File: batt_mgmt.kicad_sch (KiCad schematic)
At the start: 49 parts, among them Q1 DMN2014LHAB-7, Q2 DMP3056L, U1 BQ24074RGT, U2 BQ29728, U3 BQ27427

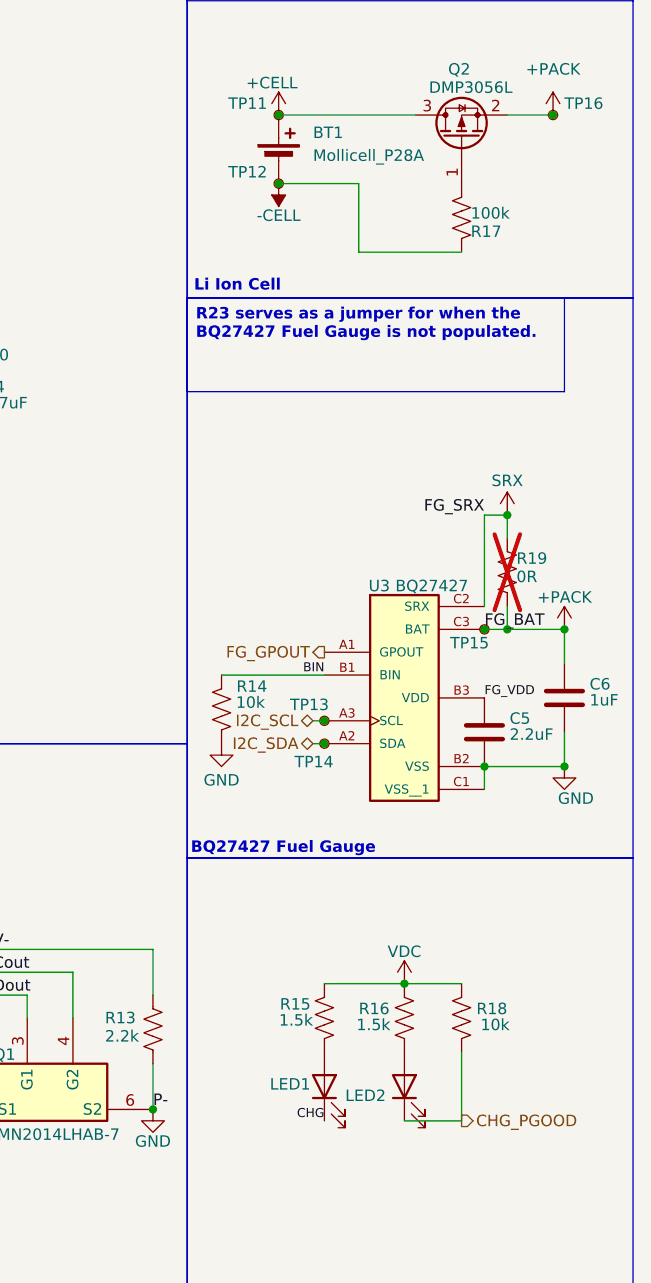
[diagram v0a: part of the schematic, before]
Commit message: Added labels and schematic PDF among other progress
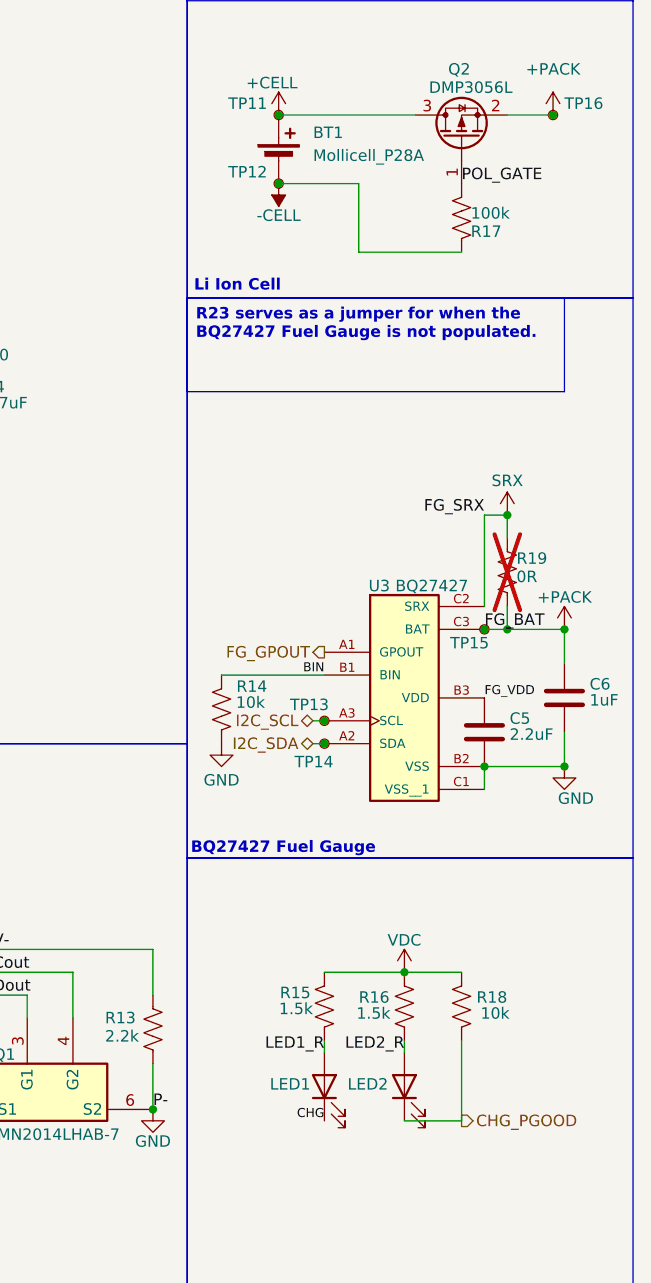
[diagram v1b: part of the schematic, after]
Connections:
- net LED2_R: now reaches LED2.2 (A), R16.1
- net LED1_R: now reaches LED1.2 (A), R15.1
- net POL_GATE: now reaches Q2.1 (G), R17.2
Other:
- moved on the sheet: R15, R16, R18
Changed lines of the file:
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@@
 	)
 	(junction
-		(at 233.68 135.89)
+		(at 233.68 134.62)
 		(diameter 0)
 		(color 0 0 0 0)
@@
 	(wire
 		(pts
-			(xy 233.68 135.89) (xy 240.03 135.89)
+			(xy 233.68 134.62) (xy 240.03 134.62)
 		)
 		(stroke
@@
 	(wire
 		(pts
-			(xy 224.79 135.89) (xy 233.68 135.89)
+			(xy 224.79 134.62) (xy 233.68 134.62)
 		)
 		(stroke
@@
 	(wire
 		(pts
+			(xy 224.79 142.24) (xy 224.79 143.51)
+		)
+		(stroke
+			(width 0)
+			(type default)
+		)
+	)
+	(wire
+		(pts
 			(xy 205.74 144.78) (xy 205.74 149.86)
 		)
@@
 	(wire
 		(pts
-			(xy 240.03 143.51) (xy 240.03 151.13)
+			(xy 240.03 142.24) (xy 240.03 151.13)
 		)
 		(stroke
@@
 	(wire
 		(pts
+			(xy 233.68 142.24) (xy 233.68 143.51)
+		)
+		(stroke
+			(width 0)
+			(type default)
+		)
+	)
+	(wire
+		(pts
 			(xy 242.57 83.82) (xy 245.11 83.82)
 		)
@@
 		)
 	)
+	(label "LED1_R"
+		(at 224.79 143.51 180)
+		(effects
+			(font
+				(size 1.27 1.27)
+			)
+			(justify right bottom)
+		)
+	)
 	(label "P-"
 		(at 205.74 149.86 0)
@@
 		)
 	)
+	(label "LED2_R"
+		(at 233.68 143.51 180)
+		(effects
+			(font
+				(size 1.27 1.27)
+			)
+			(justify right bottom)
+		)
+	)
 	(label "CHG"
 		(at 224.79 151.13 180)
@@
 		)
 	)
+	(label "POL_GATE"
+		(at 240.03 46.99 0)
+		(effects
+			(font
+				(size 1.27 1.27)
+			)
+			(justify left bottom)
+		)
+	)
 	(hierarchical_label "FG_GPOUT"
 		(shape output)
@@
 		(dnp no)
 		(property "Reference" "LED2"
-			(at 229.362 148.336 90)
+			(at 229.616 147.066 90)
 			(show_name no)
 			(do_not_autoplace no)
@@
 	(symbol
 		(lib_id "Device:R_US")
-		(at 240.03 139.7 0)
+		(at 240.03 138.43 0)
 		(mirror x)
 		(unit 1)
@@
 		(dnp no)
 		(property "Reference" "R18"
-			(at 245.11 138.684 0)
+			(at 245.11 137.414 0)
 			(show_name no)
 			(do_not_autoplace no)
@@
 		)
 		(property "Value" "10k"
-			(at 245.364 140.462 0)
+			(at 245.364 139.192 0)
 			(show_name no)
 			(do_not_autoplace no)
@@
 		)
 		(property "Footprint" "Resistor_SMD:R_0603_1608Metric"
-			(at 241.046 139.446 90)
+			(at 241.046 138.176 90)
 			(hide yes)
 			(show_name no)
@@
 		)
 		(property "Datasheet" ""
-			(at 240.03 139.7 0)
+			(at 240.03 138.43 0)
 			(hide yes)
 			(show_name no)
@@
 		)
 		(property "Description" "Resistor, US symbol"
-			(at 240.03 139.7 0)
+			(at 240.03 138.43 0)
 			(hide yes)
 			(show_name no)
@@
 		)
 		(property "MFR#" ""
-			(at 240.03 139.7 0)
+			(at 240.03 138.43 0)
 			(hide yes)
 			(show_name no)
@@
 		)
 		(property "Package" "0603"
-			(at 240.03 139.7 0)
+			(at 240.03 138.43 0)
 			(hide yes)
 			(show_name no)
@@
 		)
 		(property "LCSC#" "C98220"
-			(at 240.03 139.7 0)
+			(at 240.03 138.43 0)
 			(hide yes)
 			(show_name no)
@@
 	(symbol
 		(lib_id "Device:R_US")
-		(at 233.68 139.7 180)
+		(at 233.68 138.43 180)
 		(unit 1)
 		(body_style 1)
@@
 		(dnp no)
 		(property "Reference" "R16"
-			(at 228.6 138.684 0)
+			(at 228.6 137.414 0)
 			(show_name no)
 			(do_not_autoplace no)
@@
 		)
 		(property "Value" "1.5k"
-			(at 228.346 140.462 0)
+			(at 228.346 139.192 0)
 			(show_name no)
 			(do_not_autoplace no)
@@
 		)
 		(property "Footprint" "Resistor_SMD:R_0603_1608Metric"
-			(at 232.664 139.446 90)
+			(at 232.664 138.176 90)
 			(hide yes)
 			(show_name no)
@@
 		)
 		(property "Datasheet" ""
-			(at 233.68 139.7 0)
+			(at 233.68 138.43 0)
 			(hide yes)
 			(show_name no)
@@
 		)
 		(property "Description" "Resistor, US symbol"
-			(at 233.68 139.7 0)
+			(at 233.68 138.43 0)
 			(hide yes)
 			(show_name no)
@@
 		)
 		(property "MFR#" ""
-			(at 233.68 139.7 0)
+			(at 233.68 138.43 0)
 			(hide yes)
 			(show_name no)
@@
 		)
 		(property "Package" "0603"
-			(at 233.68 139.7 0)
+			(at 233.68 138.43 0)
 			(hide yes)
 			(show_name no)
@@
 		)
 		(property "LCSC#" "C114680"
-			(at 233.68 139.7 0)
+			(at 233.68 138.43 0)
 			(hide yes)
 			(show_name no)
@@
 	(symbol
 		(lib_id "power:VDC")
-		(at 233.68 135.89 0)
+		(at 233.68 134.62 0)
 		(unit 1)
 		(body_style 1)
@@
 		(dnp no)
 		(property "Reference" "#PWR018"
-			(at 233.68 139.7 0)
+			(at 233.68 138.43 0)
 			(hide yes)
 			(show_name no)
@@
 		)
 		(property "Value" "VDC"
-			(at 233.68 132.334 0)
+			(at 233.68 131.064 0)
 			(show_name no)
 			(do_not_autoplace no)
@@
 		)
 		(property "Footprint" ""
-			(at 233.68 135.89 0)
+			(at 233.68 134.62 0)
 			(hide yes)
 			(show_name no)
@@
 		)
 		(property "Datasheet" ""
-			(at 233.68 135.89 0)
+			(at 233.68 134.62 0)
 			(hide yes)
 			(show_name no)
@@
 		)
 		(property "Description" "Power symbol creates a global label with name \"VDC\""
-			(at 233.68 135.89 0)
+			(at 233.68 134.62 0)
 			(hide yes)
 			(show_name no)
@@
 	(symbol
 		(lib_id "Device:R_US")
-		(at 224.79 139.7 0)
+		(at 224.79 138.43 0)
 		(mirror x)
 		(unit 1)
@@
 		(dnp no)
 		(property "Reference" "R15"
-			(at 223.266 138.176 0)
+			(at 223.266 136.906 0)
 			(show_name no)
 			(do_not_autoplace no)
@@
 		)
 		(property "Value" "1.5k"
-			(at 223.52 139.954 0)
+			(at 223.52 138.684 0)
 			(show_name no)
 			(do_not_autoplace no)
@@
 		)
 		(property "Footprint" "Resistor_SMD:R_0603_1608Metric"
-			(at 225.806 139.446 90)
+			(at 225.806 138.176 90)
 			(hide yes)
 			(show_name no)
@@
 		)
 		(property "Datasheet" ""
-			(at 224.79 139.7 0)
+			(at 224.79 138.43 0)
 			(hide yes)
 			(show_name no)
@@
 		)
 		(property "Description" "Resistor, US symbol"
-			(at 224.79 139.7 0)
+			(at 224.79 138.43 0)
 			(hide yes)
 			(show_name no)
@@
 		)
 		(property "MFR#" ""
-			(at 224.79 139.7 0)
+			(at 224.79 138.43 0)
 			(hide yes)
 			(show_name no)
@@
 		)
 		(property "Package" "0603"
-			(at 224.79 139.7 0)
+			(at 224.79 138.43 0)
 			(hide yes)
 			(show_name no)
@@
 		)
 		(property "LCSC#" "C114680"
-			(at 224.79 139.7 0)
+			(at 224.79 138.43 0)
 			(hide yes)
 			(show_name no)

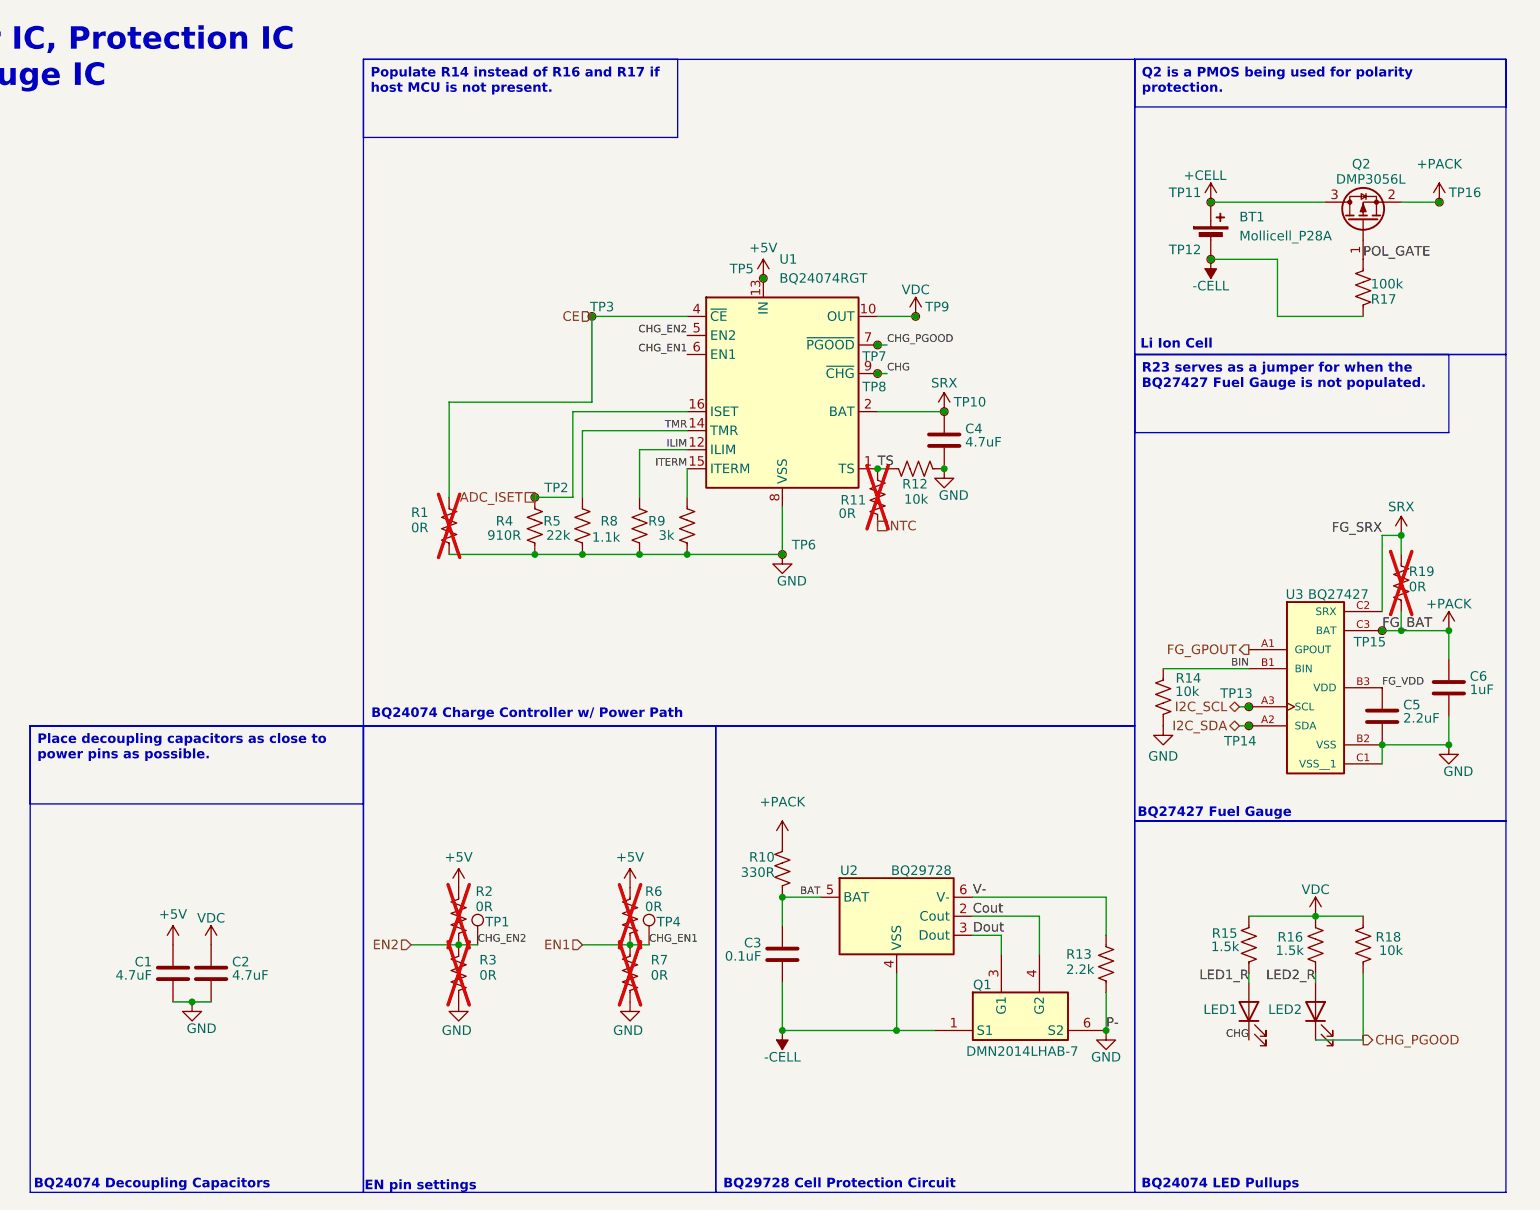
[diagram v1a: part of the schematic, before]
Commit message: Added testpoints
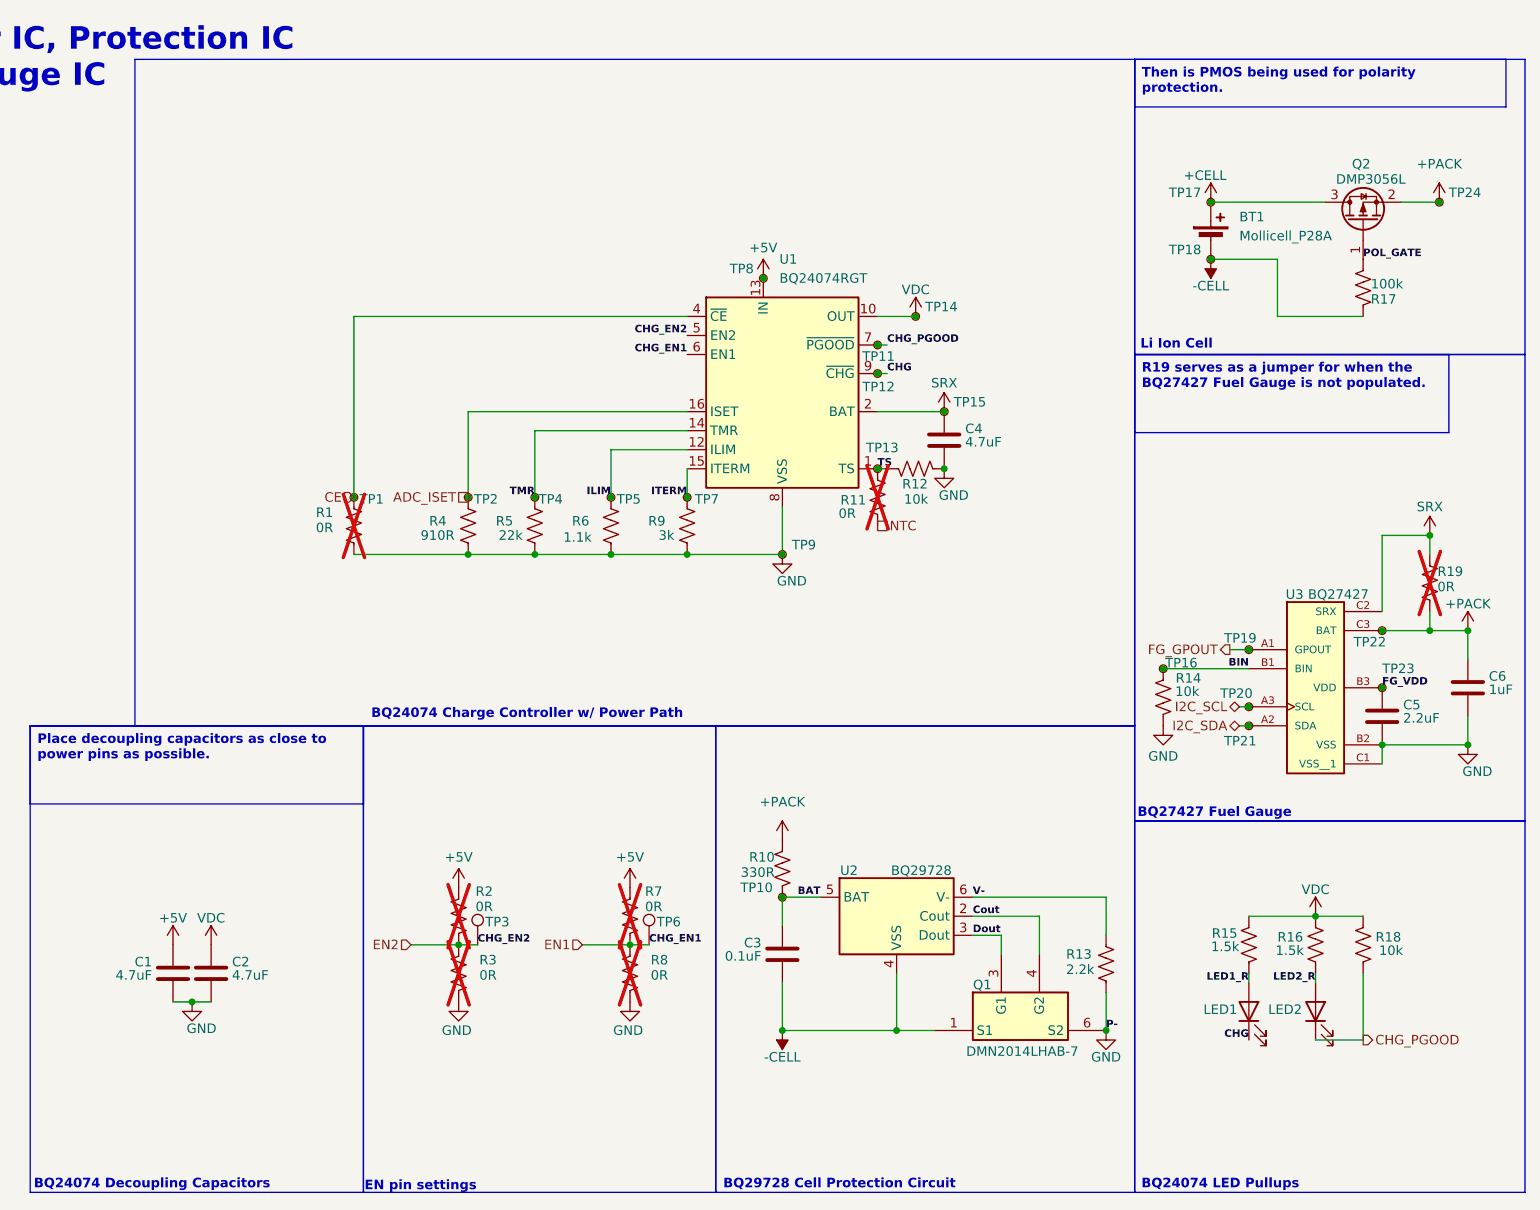
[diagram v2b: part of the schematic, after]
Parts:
- removed TP3: CE, TestPoint:TestPoint_Pad_D1.0mm, symbol Connector:TestPoint_Small
- added TP1: CE, TestPoint:TestPoint_Pad_D1.0mm, symbol Connector:TestPoint_Small
- added TP10: BAT, symbol Connector:TestPoint_Small
- added TP13: TS, symbol Connector:TestPoint_Small
- added TP16: BIN, symbol Connector:TestPoint_Small
- added TP19: FG_GPOUT, symbol Connector:TestPoint_Small
- added TP23: FG_VDD, symbol Connector:TestPoint_Small
- added TP4: TMR, symbol Connector:TestPoint_Small
- added TP5: ILIM, symbol Connector:TestPoint_Small
- added TP7: ITERM, symbol Connector:TestPoint_Small
- renumbered R8 to R6, R6 to R7, R7 to R8, TP7 to TP11, TP8 to TP12, TP9 to TP14, TP10 to TP15, TP11 to TP17, TP12 to TP18, TP13 to TP20, TP14 to TP21, TP15 to TP22, TP16 to TP24, TP1 to TP3, TP4 to TP6, TP5 to TP8, TP6 to TP9
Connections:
- net BAT: now also TP10.1
- net BIN: now also TP16.1
- net CE: now also TP1.1
- net FG_GPOUT: now also TP19.1
- net FG_VDD: now also TP23.1
- net ILIM: now also TP5.1
- net ITERM: now also TP7.1
- net TMR: now also TP4.1
- net TS: now also TP13.1
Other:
- moved on the sheet: C6, R1, R19, R4, R5, R6, TP2
